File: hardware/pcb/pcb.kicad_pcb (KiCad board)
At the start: 2 copper layers, 100 x 100 mm, 38 parts, among them Q1 FQD50N06, Q2 FQD50N06

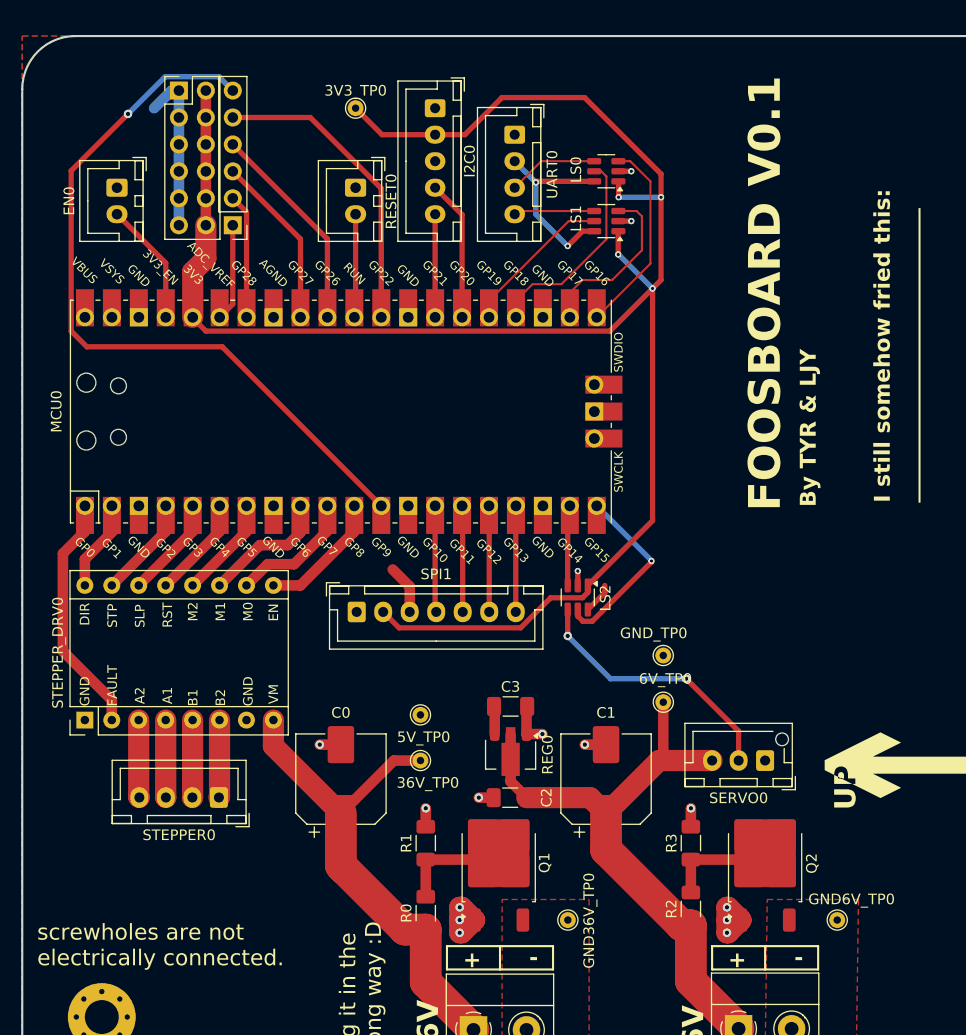
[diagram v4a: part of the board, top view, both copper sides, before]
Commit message: fixed orientations of onboard documentation
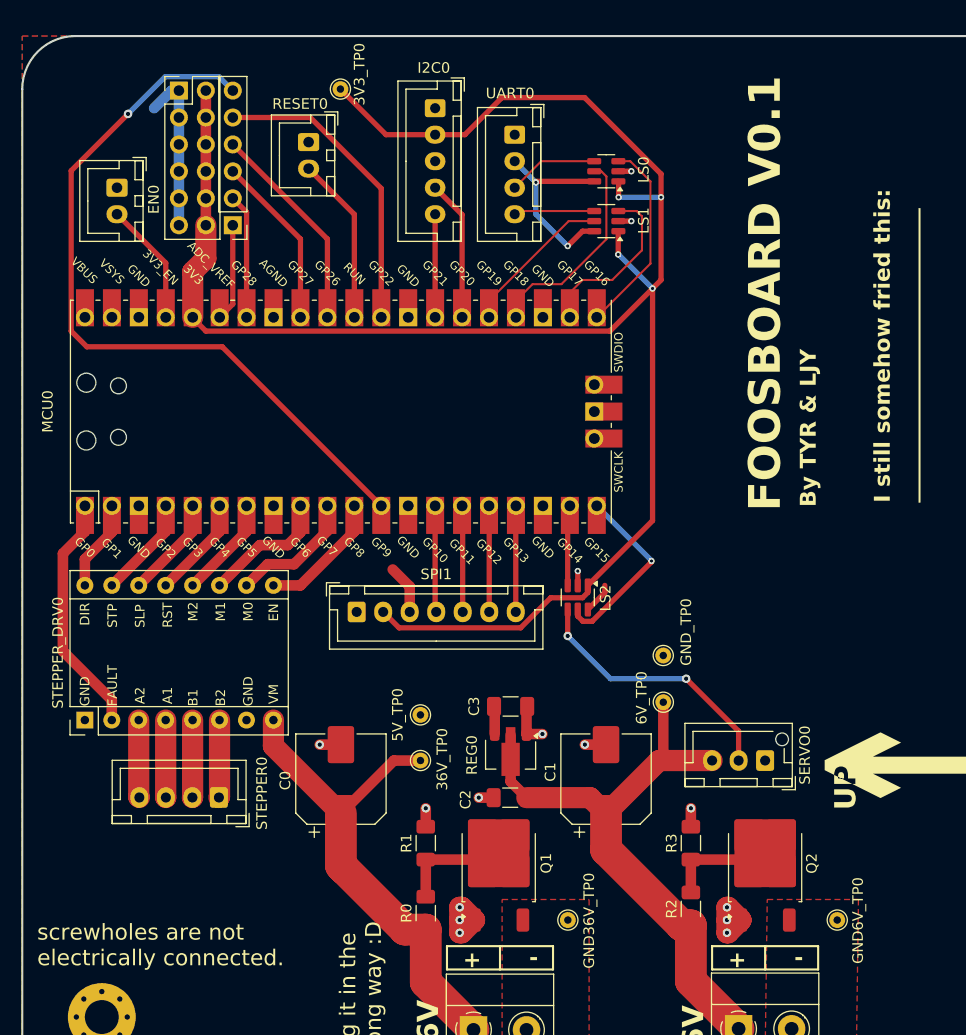
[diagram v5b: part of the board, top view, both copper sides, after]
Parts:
- moved RESET0 6.18 mm to (27.0, 10.0)
- moved 3V3_TP0 2.30 mm to (30.0, 5.00)
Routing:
- net /RESET: track 9.77 -> 15.8 mm
- net +3V3: track 181.3 -> 183.5 mm
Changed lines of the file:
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@@
 	(footprint "TestPoint:TestPoint_THTPad_D1.5mm_Drill0.7mm"
 		(layer "F.Cu")
-		(at 31.4318 6.8)
+		(at 30 5)
 		(descr "THT pad as test Point, diameter 1.5mm, hole diameter 0.7mm")
 		(tags "test point THT pad")
 		(property "Reference" "3V3_TP0"
-			(at 0 -1.648 0)
+			(at 1.8 -1.4 90)
 			(layer "F.SilkS")
 			(effects
@@
 		(tags "test point THT pad")
 		(property "Reference" "GND_TP0"
-			(at -2.1 0.9 360)
+			(at -2.21 -2.1582 90)
 			(layer "F.SilkS")
 			(effects
@@
 		(tags "SOT-89-3")
 		(property "Reference" "REG0"
-			(at 0 -3.5 90)
+			(at 0.035 3.6468 90)
 			(layer "F.SilkS")
 			(effects
@@
 		(tags "SOT TO_SOT_SMD")
 		(property "Reference" "LS0"
-			(at 2.8375 0.15 90)
+			(at -3.5307 0.15 90)
 			(layer "F.SilkS")
 			(effects
@@
 		(tags "connector JST XH vertical boss")
 		(property "Reference" "SERVO0"
-			(at 2.5 -3.55 360)
+			(at -3.7532 0.515 90)
 			(layer "F.SilkS")
 			(effects
@@
 		(tags "capacitor handsolder")
 		(property "Reference" "C3"
-			(at 0 -1.85 360)
+			(at -3.4468 -0.015 90)
 			(layer "F.SilkS")
 			(effects
@@
 		(tags "Through hole pin header THT 2x20 2.54mm double row")
 		(property "Reference" "MCU0"
-			(at 0.01 -26.81 90)
+			(at 0.01 -27.6418 90)
 			(layer "F.SilkS")
 			(effects
@@
 	(footprint "Connector_JST:JST_XH_B2B-XH-A_1x02_P2.50mm_Vertical"
 		(layer "F.Cu")
-		(at 31.4318 14.3 -90)
+		(at 27 10 -90)
 		(descr "JST XH series connector, B2B-XH-A (http://www.jst-mfg.com/product/pdf/eng/eXH.pdf), generated with kicad-footprint-generator")
 		(tags "connector JST XH vertical")
 		(property "Reference" "RESET0"
-			(at 1.3 -3.3682 90)
+			(at -3.6 0.8 180)
 			(layer "F.SilkS")
 			(effects
@@
 		(tags "connector JST XH vertical")
 		(property "Reference" "UART0"
-			(at 3.75 -3.55 -90)
+			(at -3.9 0.4318 180)
 			(layer "F.SilkS")
 			(effects
@@
 		(tags "connector JST XH vertical")
 		(property "Reference" "EN0"
-			(at 1.25 4.5 90)
+			(at 1.1 -3.4682 90)
 			(layer "F.SilkS")
 			(effects
@@
 		(tags "capacitor handsolder")
 		(property "Reference" "C2"
-			(at -3.4375 0 90)
+			(at 4.2093 -0.185 90)
 			(layer "F.SilkS")
 			(effects
@@
 		(tags "connector JST XH vertical")
 		(property "Reference" "STEPPER0"
-			(at 3.75 -3.55 180)
+			(at -4.0582 0.4 -90)
 			(layer "F.SilkS")
 			(effects
@@
 		(tags "test point THT pad")
 		(property "Reference" "36V_TP0"
-			(at -2.1 0.7 360)
+			(at 0.115 2.0532 90)
 			(layer "F.SilkS")
 			(effects
@@
 		(tags "test point THT pad")
 		(property "Reference" "6V_TP0"
-			(at 2.2 0.2 360)
+			(at 0.415 -2.0468 90)
 			(layer "F.SilkS")
 			(effects
@@
 		(tags "capacitor electrolytic")
 		(property "Reference" "C1"
-			(at 6.25 0 360)
+			(at 0.665 -5.2468 90)
 			(layer "F.SilkS")
 			(effects
@@
 		(tags "DPAK TO-252 DPAK-3 TO-252-3 SOT-428")
 		(property "Reference" "Q1"
-			(at 0.36 4.32 90)
+			(at 0.315 4.4732 90)
 			(layer "F.SilkS")
 			(effects
@@
 		(tags "test point THT pad")
 		(property "Reference" "5V_TP0"
-			(at -2.1 0.3 360)
+			(at 0.01 -2.1468 90)
 			(layer "F.SilkS")
 			(effects
@@
 		(tags "test point THT pad")
 		(property "Reference" "GND6V_TP0"
-			(at 1.3532 -1.955 360)
+			(at 1.9532 0.045 90)
 			(layer "F.SilkS")
 			(effects
@@
 		(tags "connector JST XH vertical")
 		(property "Reference" "I2C0"
-			(at 5 -3.2682 -90)
+			(at -3.8 0.1318 0)
 			(layer "F.SilkS")
 			(effects
@@
 		(tags "SOT TO_SOT_SMD")
 		(property "Reference" "LS1"
-			(at 2.8375 0.25 90)
+			(at -3.5307 0.05 90)
 			(layer "F.SilkS")
 			(effects
@@
 		(tags "capacitor electrolytic")
 		(property "Reference" "C0"
-			(at 6.25 0 360)
+			(at -0.135 -5.2468 90)
 			(layer "F.SilkS")
 			(effects
@@
 		)
 	)
-	(gr_text_box "GND|3V3"
-		(start 13.3918 0.9)
-		(end 21.1318 3.31)
-		(layer "F.SilkS")
+	(gr_text_box "P09|P22|P26|P27|P28|AVREF"
+		(start 21 1.0619)
+		(end 23.4 22.9381)
+		(angle 90)
+		(layer "B.SilkS")
 		(effects
 			(font
@@
 				(bold yes)
 			)
-			(justify top)
+			(justify top mirror)
 		)
 		(border yes)
@@
 		)
 	)
-	(gr_text_box "GND|CTRL|6V"
-		(start 62.507 62.015)
-		(end 72.523 64.415)
-		(angle 180)
+	(gr_text_box "GND|3V3"
+		(start 12.7959 0.9)
+		(end 19.2041 3.31)
 		(layer "F.SilkS")
 		(effects
@@
 		)
 	)
-	(gr_text_box "SCL|SDA|3V3|5V|GND"
-		(start 26.0222 0.9)
-		(end 41.8414 3.3)
+	(gr_text_box "6V|CTRL|GND"
+		(start 62.507 62.015)
+		(end 72.523 64.415)
 		(layer "F.SilkS")
 		(effects
@@
 		)
 	)
-	(gr_text_box "GND|3V3|5V|SCK|MOSI|MISO|SCS"
-		(start 26.8278 58.2)
-		(end 51.2358 60.392)
+	(gr_text_box "SCL|SDA|3V3|5V|GND"
+		(start 32.6 3.8904)
+		(end 35 19.7096)
+		(angle 90)
 		(layer "F.SilkS")
 		(effects
@@
 		)
 	)
-	(gr_text_box "TX|RX|5V|GND"
-		(start 42.6222 2.6)
-		(end 53.8414 5)
+	(gr_text_box "GND|3V3|5V|SCK|MOSI|MISO|SCS"
+		(start 26.8278 58.2)
+		(end 51.2358 60.392)
 		(layer "F.SilkS")
 		(effects
@@
 		)
 	)
-	(gr_text_box "RESET|GND"
-		(start 26.4159 8.8159)
-		(end 34.8477 11.2159)
+	(gr_text_box "TX|RX|5V|GND"
+		(start 49.6 7.3904)
+		(end 52 18.6096)
+		(angle 90)
 		(layer "F.SilkS")
 		(effects
@@
 		)
 	)
-	(gr_text_box "VREF|GP28|GP27|GP26|GP22|GP9"
-		(start 0.9318 3.9)
-		(end 3.3318 29.1762)
+	(gr_text_box "RESET|GND"
+		(start 29.96 7.0341)
+		(end 32.36 15.4659)
 		(angle 90)
 		(layer "F.SilkS")
@@
 	)
 	(gr_text_box "EN|GND"
-		(start 5 8.8)
-		(end 11.8318 11.2)
+		(start 2.6 12.1841)
+		(end 5 19.0159)
+		(angle 90)
 		(layer "F.SilkS")
 		(effects
@@
 	)
 	(segment
-		(start 33.9318 9.3)
-		(end 31.4318 6.8)
-		(width 0.5)
-		(layer "F.Cu")
-		(net 19)
-	)
-	(segment
 		(start 17.3118 17.84)
 		(end 17.3118 20.98)
@@
 	(segment
 		(start 38.9318 9.3)
-		(end 33.9318 9.3)
+		(end 34.3 9.3)
 		(width 0.5)
 		(layer "F.Cu")
@@
 	)
 	(segment
+		(start 34.3 9.3)
+		(end 30 5)
+		(width 0.5)
+		(layer "F.Cu")
+		(net 19)
+	)
+	(segment
 		(start 56.194658 18.412142)
 		(end 56.2068 18.4)
@@
 	)
 	(segment
-		(start 31.3118 26.52)
-		(end 31.4318 26.4)
+		(start 27 12.5)
+		(end 31.3118 16.8118)
 		(width 0.5)
 		(layer "F.Cu")
@@
 	)
 	(segment
-		(start 31.4318 26.4)
-		(end 31.4318 16.8)
+		(start 31.3118 16.8118)
+		(end 31.3118 26.52)
 		(width 0.5)
 		(layer "F.Cu")

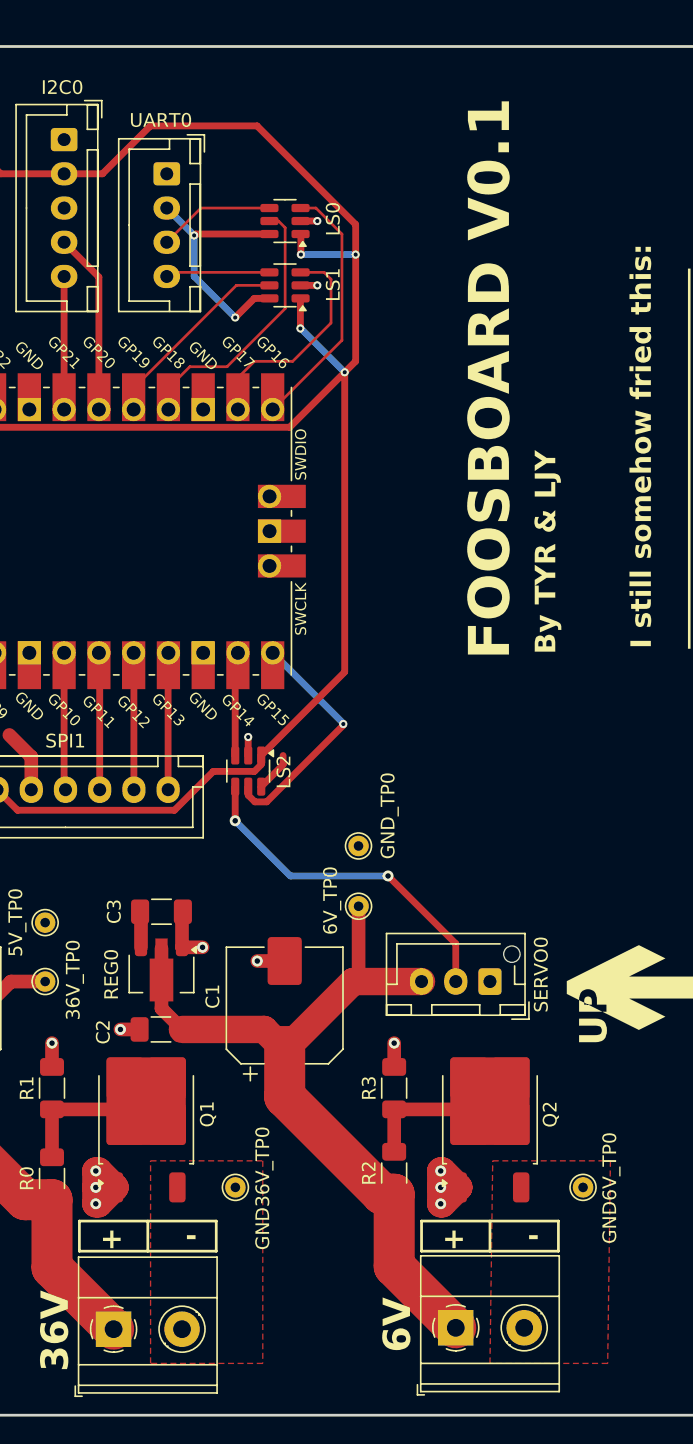
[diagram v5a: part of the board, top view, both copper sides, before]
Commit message: fixed my stupid mistake, reverse polarity protection should work now
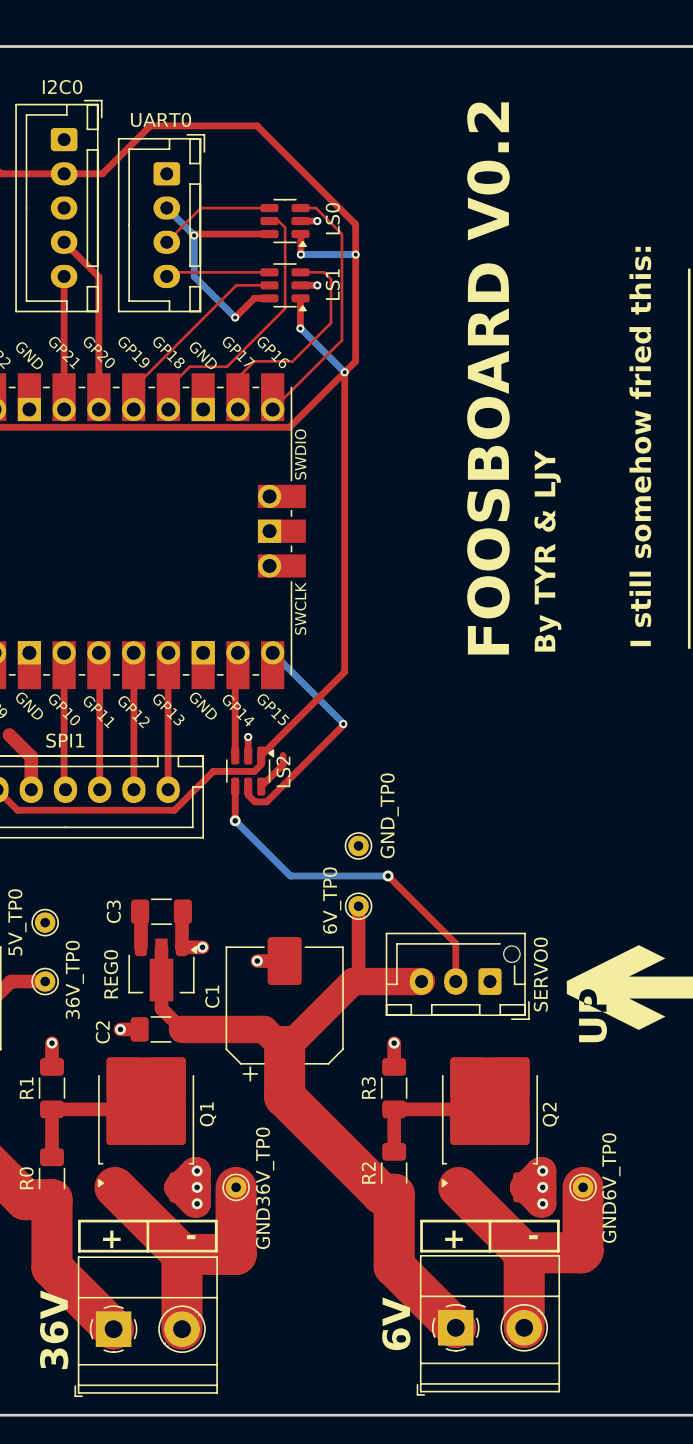
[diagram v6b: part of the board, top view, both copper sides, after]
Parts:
- moved GND36V_TP0 0.05 mm to (51.5, 83.4)
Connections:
- Q1 pad 1: GND -> GND36V
- Q1 pad 3: GND36V -> GND
- Q2 pad 1: GND -> GND6V
- Q2 pad 3: GND6V -> GND
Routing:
- net GND36V: track 0.00 -> 21.2 mm
- net GND6V: track 0.00 -> 21.2 mm
- removed copper zone on F.Cu, net GND36V
- removed copper zone on F.Cu, net GND6V
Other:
- board text added: "FOOSBOARD V0.2"
- board text removed: "FOOSBOARD V0.1"
